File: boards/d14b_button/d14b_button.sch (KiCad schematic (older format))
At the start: 31 parts, among them SW1 SW_PUSH, SW2 SW_PUSH, U2 nRF24L01+-Module

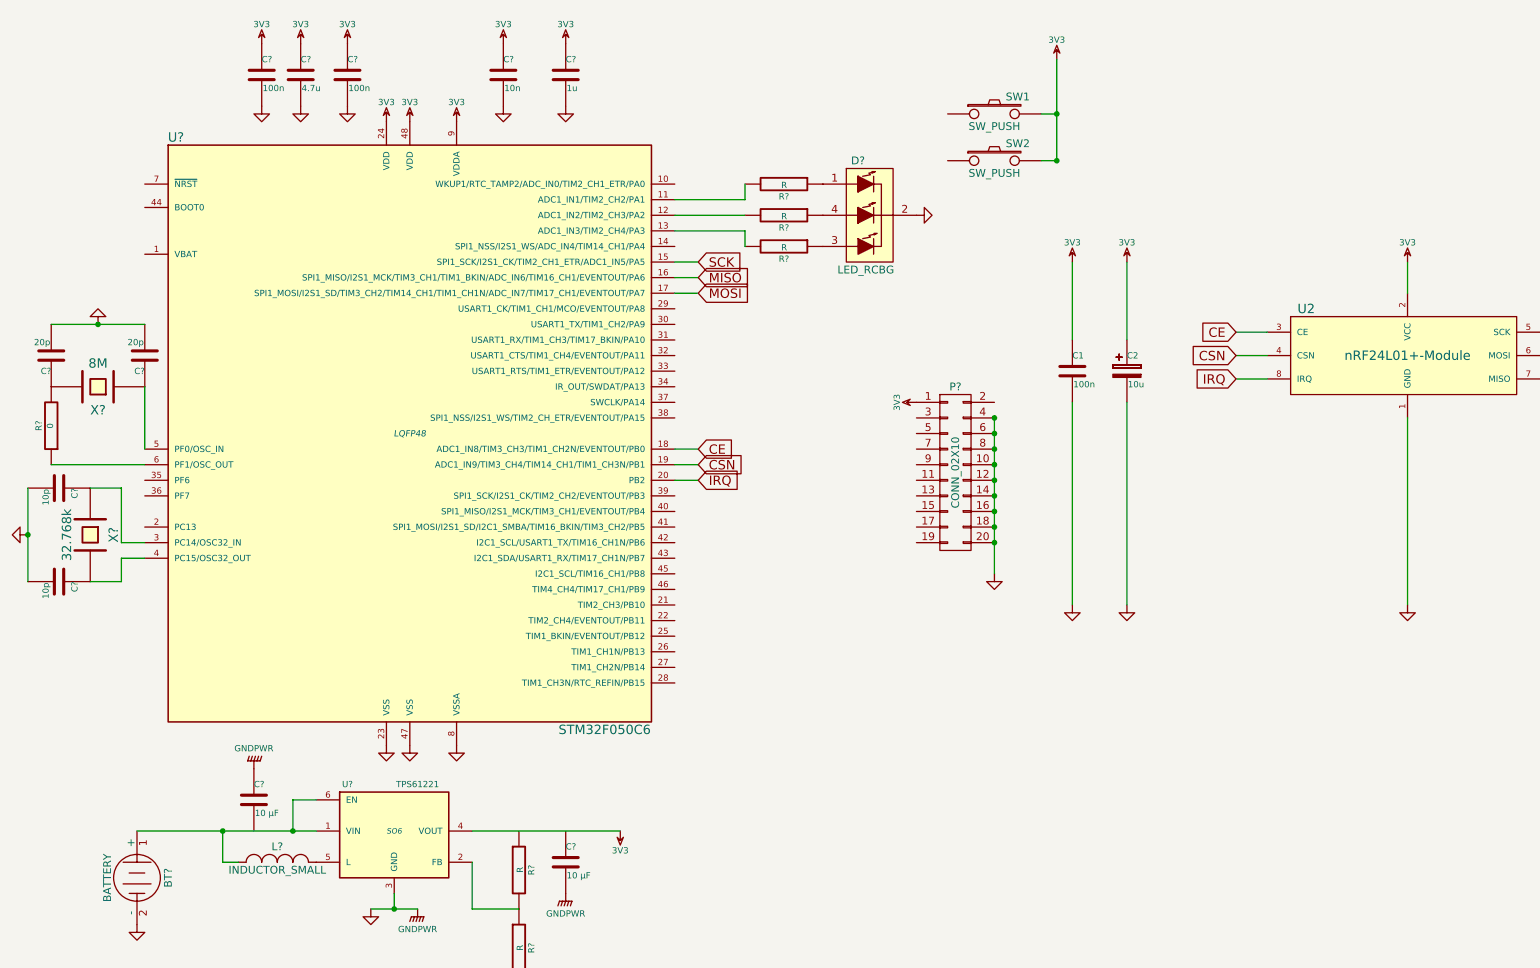
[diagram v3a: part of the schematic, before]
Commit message: 3V3-Label überarbeitet und BOOT0-Selektor hinzugefügt
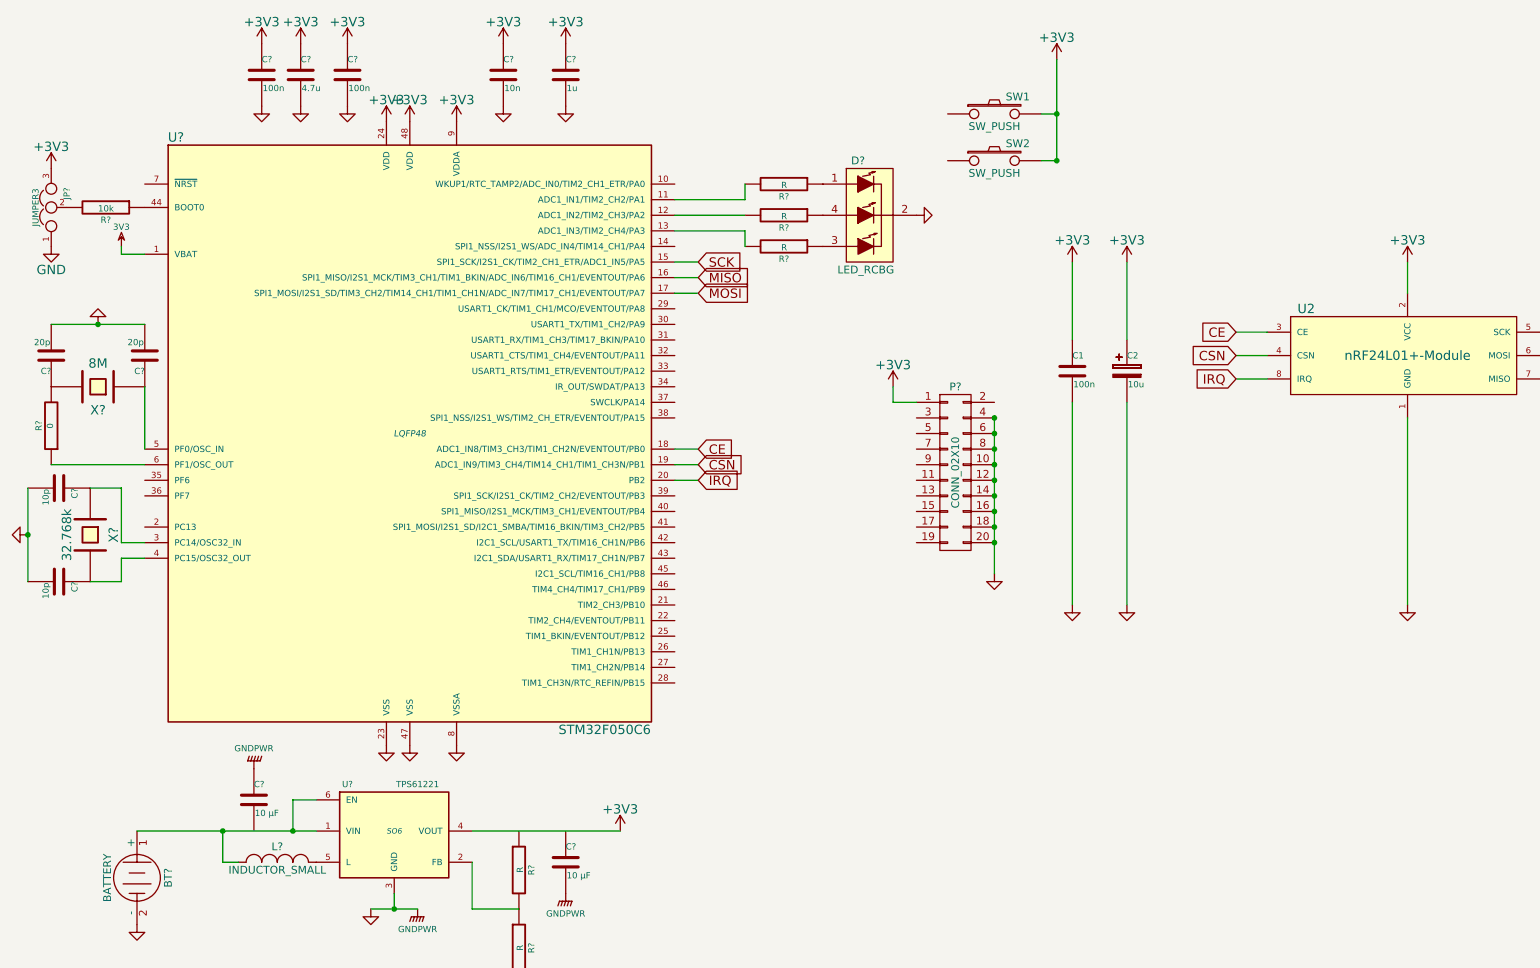
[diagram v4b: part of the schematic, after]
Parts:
- added JP?: JUMPER3, symbol JUMPER3
- added R?: 10k, symbol R
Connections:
- net 3V3: now also U?.1 (VBAT); no longer C1.1, C2.1, C?.1, C?.1, C?.1, C?.1, C?.1, P?.1 (P1), SW1.2, SW2.2, U2.2 (VCC), U?.24 (VDD), U?.4 (VOUT), U?.48 (VDD), U?.9 (VDDA)
- net GND: now also JP?.1
- net at U?.44 (BOOT0): now also R?.1
- new net: JP?.2, R?.2
- new net +3V3: C1.1, C2.1, C?.1, C?.1, C?.1, C?.1, C?.1, JP?.3, P?.1 (P1), SW1.2, SW2.2, U2.2 (VCC), U?.24 (VDD), U?.4 (VOUT), U?.48 (VDD), U?.9 (VDDA)
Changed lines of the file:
@@
-	1    0    0    -1
-$EndComp
-$Comp
-L 3V3 #PWR03
-U 1 1 54807252
-P 9450 2100
-F 0 "#PWR03" H 9450 2200 40  0001 C CNN
-F 1 "3V3" H 9450 2225 40  0000 C CNN
-F 2 "" H 9450 2100 60  0000 C CNN
-F 3 "" H 9450 2100 60  0000 C CNN
-	1    9450 2100
-	1    0    0    -1
-$EndComp
-$Comp
-L 3V3 #PWR04
-U 1 1 5480734E
-P 2900 1200
-F 0 "#PWR04" H 2900 1300 40  0001 C CNN
-F 1 "3V3" H 2900 1325 40  0000 C CNN
-F 2 "" H 2900 1200 60  0000 C CNN
-F 3 "" H 2900 1200 60  0000 C CNN
-	1    2900 1200
 	1    0    0    -1
 $EndComp
@@
 	7200 1450 7100 1450
 Connection ~ 7200 1450
-$Comp
-L 3V3 #PWR05
-U 1 1 5480A257
-P 7200 800
-F 0 "#PWR05" H 7200 900 40  0001 C CNN
-F 1 "3V3" H 7200 925 40  0000 C CNN
-F 2 "" H 7200 800 60  0000 C CNN
-F 3 "" H 7200 800 60  0000 C CNN
-	1    7200 800
-	1    0    0    -1
-$EndComp
 Wire Wire Line
 	8550 2550 8350 2550
@@
 F 3 "" H 7300 2800 60  0000 C CNN
 	1    7300 2800
-	1    0    0    -1
-$EndComp
-$Comp
-L 3V3 #PWR06
-U 1 1 5480AE60
-P 7300 2100
-F 0 "#PWR06" H 7300 2200 40  0001 C CNN
-F 1 "3V3" H 7300 2225 40  0000 C CNN
-F 2 "" H 7300 2100 60  0000 C CNN
-F 3 "" H 7300 2100 60  0000 C CNN
-	1    7300 2100
-	1    0    0    -1
-$EndComp
-$Comp
-L 3V3 #PWR07
-U 1 1 5480AE73
-P 7650 2100
-F 0 "#PWR07" H 7650 2200 40  0001 C CNN
-F 1 "3V3" H 7650 2225 40  0000 C CNN
-F 2 "" H 7650 2100 60  0000 C CNN
-F 3 "" H 7650 2100 60  0000 C CNN
-	1    7650 2100
 	1    0    0    -1
 $EndComp
@@
 $EndComp
 $Comp
-L 3V3 #PWR?
-U 1 1 54AF9F2F
-P 2350 700
-F 0 "#PWR?" H 2350 800 40  0001 C CNN
-F 1 "3V3" H 2350 825 40  0000 C CNN
-F 2 "" H 2350 700 60  0000 C CNN
-F 3 "" H 2350 700 60  0000 C CNN
-	1    2350 700
-	1    0    0    -1
-$EndComp
-$Comp
-L 3V3 #PWR?
-U 1 1 54AF9F50
-P 2650 700
-F 0 "#PWR?" H 2650 800 40  0001 C CNN
-F 1 "3V3" H 2650 825 40  0000 C CNN
-F 2 "" H 2650 700 60  0000 C CNN
-F 3 "" H 2650 700 60  0000 C CNN
-	1    2650 700
-	1    0    0    -1
-$EndComp
-$Comp
-L 3V3 #PWR?
-U 1 1 54AF9F71
-P 3650 700
-F 0 "#PWR?" H 3650 800 40  0001 C CNN
-F 1 "3V3" H 3650 825 40  0000 C CNN
-F 2 "" H 3650 700 60  0000 C CNN
-F 3 "" H 3650 700 60  0000 C CNN
-	1    3650 700
-	1    0    0    -1
-$EndComp
-$Comp
-L 3V3 #PWR?
-U 1 1 54AF9F92
-P 4050 700
-F 0 "#PWR?" H 4050 800 40  0001 C CNN
-F 1 "3V3" H 4050 825 40  0000 C CNN
-F 2 "" H 4050 700 60  0000 C CNN
-F 3 "" H 4050 700 60  0000 C CNN
-	1    4050 700
-	1    0    0    -1
-$EndComp
-$Comp
 L GND #PWR?
 U 1 1 54AFA0D1
@@
 F 3 "" H 4050 1100 60  0000 C CNN
 	1    4050 1100
-	1    0    0    -1
-$EndComp
-$Comp
-L 3V3 #PWR?
-U 1 1 54AFA225
-P 3350 1200
-F 0 "#PWR?" H 3350 1300 40  0001 C CNN
-F 1 "3V3" H 3350 1325 40  0000 C CNN
-F 2 "" H 3350 1200 60  0000 C CNN
-F 3 "" H 3350 1200 60  0000 C CNN
-	1    3350 1200
 	1    0    0    -1
 $EndComp
@@
 $EndComp
 $Comp
-L 3V3 #PWR?
-U 1 1 54AFD954
-P 6300 3000
-F 0 "#PWR?" H 6300 3100 40  0001 C CNN
-F 1 "3V3" H 6300 3125 40  0000 C CNN
-F 2 "" H 6300 3000 60  0000 C CNN
-F 3 "" H 6300 3000 60  0000 C CNN
-	1    6300 3000
-	0    -1   -1   0
-$EndComp
-$Comp
 L STM32F050C6 U?
 U 1 1 54AFE9EC
@@
 $EndComp
 $Comp
-L 3V3 #PWR?
-U 1 1 54B015C2
-P 3050 1200
-F 0 "#PWR?" H 3050 1300 40  0001 C CNN
-F 1 "3V3" H 3050 1325 40  0000 C CNN
-F 2 "" H 3050 1200 60  0000 C CNN
-F 3 "" H 3050 1200 60  0000 C CNN
-	1    3050 1200
-	1    0    0    -1
-$EndComp
-$Comp
 L C C?
 U 1 1 54B015E8
@@
 	1    0    0    -1
 $EndComp
-$Comp
-L 3V3 #PWR?
-U 1 1 54B0168E
-P 2100 700
-F 0 "#PWR?" H 2100 800 40  0001 C CNN
-F 1 "3V3" H 2100 825 40  0000 C CNN
-F 2 "" H 2100 700 60  0000 C CNN
-F 3 "" H 2100 700 60  0000 C CNN
-	1    2100 700
-	1    0    0    -1
-$EndComp
 Wire Wire Line
 	4750 1700 5200 1700
@@
 Wire Wire Line
 	5200 1900 5200 2000
-$Comp
-L 3V3 #PWR?
-U 1 1 54B07DA2
-P 4400 5750
-F 0 "#PWR?" H 4400 5850 40  0001 C CNN
-F 1 "3V3" H 4400 5875 40  0000 C CNN
-F 2 "" H 4400 5750 60  0000 C CNN
-F 3 "" H 4400 5750 60  0000 C CNN
-	1    4400 5750
-	-1   0    0    1
-$EndComp
 $Comp
 L GND #PWR?
@@
 Wire Wire Line
 	1200 4150 1000 4150
+$Comp
+L 3V3 #PWR?
+U 1 1 54AFD499
+P 1200 2000
+F 0 "#PWR?" H 1200 2100 40  0001 C CNN
+F 1 "3V3" H 1200 2125 40  0000 C CNN
+F 2 "" H 1200 2000 60  0000 C CNN
+F 3 "" H 1200 2000 60  0000 C CNN
+	1    1200 2000
+	1    0    0    -1
+$EndComp
+Wire Wire Line
+	1200 2000 1200 2050
+Wire Wire Line
+	1200 2050 1350 2050
+$Comp
+L JUMPER3 JP?
+U 1 1 54AFD79C
+P 750 1750
+F 0 "JP?" H 800 1650 40  0000 L CNN
+F 1 "JUMPER3" H 750 1850 40  0000 C CNN
+F 2 "" H 750 1750 60  0000 C CNN
+F 3 "" H 750 1750 60  0000 C CNN
+	1    750  1750
+	0    -1   -1   0
+$EndComp
+$Comp
+L R R?
+U 1 1 54AFD7FD
+P 1100 1750
+F 0 "R?" V 1180 1750 40  0000 C CNN
+F 1 "10k" V 1107 1751 40  0000 C CNN
+F 2 "" V 1030 1750 30  0000 C CNN
+F 3 "" H 1100 1750 30  0000 C CNN
+	1    1100 1750
+	0    1    1    0
+$EndComp
+$Comp
+L GND #PWR?
+U 1 1 54AFD975
+P 750 2000
+F 0 "#PWR?" H 750 1750 60  0001 C CNN
+F 1 "GND" H 750 1850 60  0000 C CNN
+F 2 "" H 750 2000 60  0000 C CNN
+F 3 "" H 750 2000 60  0000 C CNN
+	1    750  2000
+	1    0    0    -1
+$EndComp
+$Comp
+L +3V3 #PWR?
+U 1 1 54AFD989
+P 750 1500
+F 0 "#PWR?" H 750 1350 60  0001 C CNN
+F 1 "+3V3" H 750 1640 60  0000 C CNN
+F 2 "" H 750 1500 60  0000 C CNN
+F 3 "" H 750 1500 60  0000 C CNN
+	1    750  1500
+	1    0    0    -1
+$EndComp
+$Comp
+L +3V3 #PWR?
+U 1 1 54AFDA66
+P 2100 700
+F 0 "#PWR?" H 2100 550 60  0001 C CNN
+F 1 "+3V3" H 2100 840 60  0000 C CNN
+F 2 "" H 2100 700 60  0000 C CNN
+F 3 "" H 2100 700 60  0000 C CNN
+	1    2100 700
+	1    0    0    -1
+$EndComp
+$Comp
+L +3V3 #PWR?
+U 1 1 54AFDA99
+P 2350 700
+F 0 "#PWR?" H 2350 550 60  0001 C CNN
+F 1 "+3V3" H 2350 840 60  0000 C CNN
+F 2 "" H 2350 700 60  0000 C CNN
+F 3 "" H 2350 700 60  0000 C CNN
+	1    2350 700
+	1    0    0    -1
+$EndComp
+$Comp
+L +3V3 #PWR?
+U 1 1 54AFDAC5
+P 2650 700
+F 0 "#PWR?" H 2650 550 60  0001 C CNN
+F 1 "+3V3" H 2650 840 60  0000 C CNN
+F 2 "" H 2650 700 60  0000 C CNN
+F 3 "" H 2650 700 60  0000 C CNN
+	1    2650 700
+	1    0    0    -1
+$EndComp
+$Comp
+L +3V3 #PWR?
+U 1 1 54AFE3DB
+P 2900 1200
+F 0 "#PWR?" H 2900 1050 60  0001 C CNN
+F 1 "+3V3" H 2900 1340 60  0000 C CNN
+F 2 "" H 2900 1200 60  0000 C CNN
+F 3 "" H 2900 1200 60  0000 C CNN
+	1    2900 1200
+	1    0    0    -1
+$EndComp
+$Comp
+L +3V3 #PWR?
+U 1 1 54AFE407
+P 3050 1200
+F 0 "#PWR?" H 3050 1050 60  0001 C CNN
+F 1 "+3V3" H 3050 1340 60  0000 C CNN
+F 2 "" H 3050 1200 60  0000 C CNN
+F 3 "" H 3050 1200 60  0000 C CNN
+	1    3050 1200
+	1    0    0    -1
+$EndComp
+$Comp
+L +3V3 #PWR?
+U 1 1 54AFE433
+P 3350 1200
+F 0 "#PWR?" H 3350 1050 60  0001 C CNN
+F 1 "+3V3" H 3350 1340 60  0000 C CNN
+F 2 "" H 3350 1200 60  0000 C CNN
+F 3 "" H 3350 1200 60  0000 C CNN
+	1    3350 1200
+	1    0    0    -1
+$EndComp
+$Comp
+L +3V3 #PWR?
+U 1 1 54AFE45F
+P 3650 700
+F 0 "#PWR?" H 3650 550 60  0001 C CNN
+F 1 "+3V3" H 3650 840 60  0000 C CNN
+F 2 "" H 3650 700 60  0000 C CNN
+F 3 "" H 3650 700 60  0000 C CNN
+	1    3650 700
+	1    0    0    -1
+$EndComp
+$Comp
+L +3V3 #PWR?
+U 1 1 54AFE48B
+P 4050 700
+F 0 "#PWR?" H 4050 550 60  0001 C CNN
+F 1 "+3V3" H 4050 840 60  0000 C CNN
+F 2 "" H 4050 700 60  0000 C CNN
+F 3 "" H 4050 700 60  0000 C CNN
+	1    4050 700
+	1    0    0    -1
+$EndComp
+$Comp
+L +3V3 #PWR?
+U 1 1 54AFE5A1
+P 7200 800
+F 0 "#PWR?" H 7200 650 60  0001 C CNN
+F 1 "+3V3" H 7200 940 60  0000 C CNN
+F 2 "" H 7200 800 60  0000 C CNN
+F 3 "" H 7200 800 60  0000 C CNN
+	1    7200 800
+	1    0    0    -1
+$EndComp
+$Comp
+L +3V3 #PWR?
+U 1 1 54AFE8D8
+P 7300 2100
+F 0 "#PWR?" H 7300 1950 60  0001 C CNN
+F 1 "+3V3" H 7300 2240 60  0000 C CNN
+F 2 "" H 7300 2100 60  0000 C CNN
+F 3 "" H 7300 2100 60  0000 C CNN
+	1    7300 2100
+	1    0    0    -1
+$EndComp
+$Comp
+L +3V3 #PWR?
+U 1 1 54AFE90B
+P 7650 2100
+F 0 "#PWR?" H 7650 1950 60  0001 C CNN
+F 1 "+3V3" H 7650 2240 60  0000 C CNN
+F 2 "" H 7650 2100 60  0000 C CNN
+F 3 "" H 7650 2100 60  0000 C CNN
+	1    7650 2100
+	1    0    0    -1
+$EndComp
+$Comp
+L +3V3 #PWR?
+U 1 1 54AFE9BC
+P 9450 2100
+F 0 "#PWR?" H 9450 1950 60  0001 C CNN
+F 1 "+3V3" H 9450 2240 60  0000 C CNN
+F 2 "" H 9450 2100 60  0000 C CNN
+F 3 "" H 9450 2100 60  0000 C CNN
+	1    9450 2100
+	1    0    0    -1
+$EndComp
+$Comp
+L +3V3 #PWR?
+U 1 1 54AFEB56
+P 6150 2900
+F 0 "#PWR?" H 6150 2750 60  0001 C CNN
+F 1 "+3V3" H 6150 3040 60  0000 C CNN
+F 2 "" H 6150 2900 60  0000 C CNN
+F 3 "" H 6150 2900 60  0000 C CNN
+	1    6150 2900
+	1    0    0    -1
+$EndComp
+Wire Wire Line
+	6150 2900 6150 3000
+Wire Wire Line
+	6150 3000 6300 3000
+$Comp
+L +3V3 #PWR?
+U 1 1 54AFEE44
+P 4400 5750
+F 0 "#PWR?" H 4400 5600 60  0001 C CNN
+F 1 "+3V3" H 4400 5890 60  0000 C CNN
+F 2 "" H 4400 5750 60  0000 C CNN
+F 3 "" H 4400 5750 60  0000 C CNN
+	1    4400 5750
+	1    0    0    -1
+$EndComp
 $EndSCHEMATC

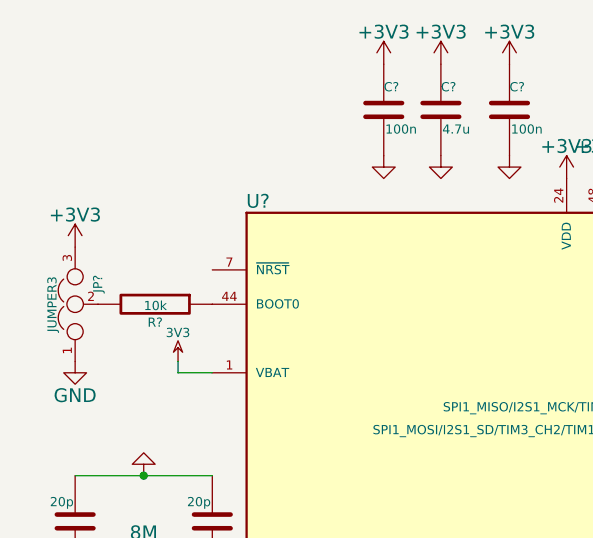
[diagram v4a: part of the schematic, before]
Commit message: VBAT über Brücke angebunden, um evtl später Dinge ändern zu können
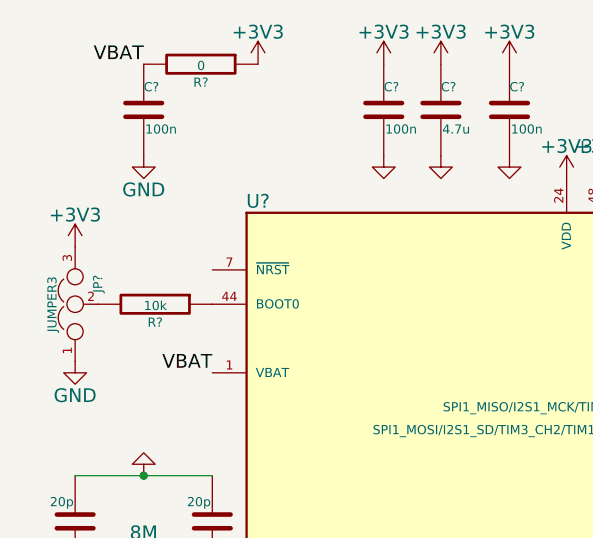
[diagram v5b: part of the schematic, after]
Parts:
- added C?: 100n, symbol C
- added R?: 0, symbol R
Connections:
- net +3V3: now also R?.1
- net GND: now also C?.2
- net 3V3 renamed VBAT
- net VBAT: now also C?.1, R?.2
